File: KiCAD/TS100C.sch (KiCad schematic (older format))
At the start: 63 parts, among them J1 USB_C_Receptacle_USB2.0, J2 OLED_64x32, J3 A, J4 B, J5 DNP, P1 TC2030-CTX, Q1 SS8050, Q2 DMP3017SFG, SW1 key1, SW2 key2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

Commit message: fixed STM
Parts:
- U4: value STM32F072C8Ux -> STM32F072CBUx
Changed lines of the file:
@@
 EESchema Schematic File Version 4
 LIBS:TS100C-cache
-EELAYER 26 0
+EELAYER 30 0
 EELAYER END
 $Descr A3 16535 11693
@@
 P 7450 2700
 F 0 "U4" H 6900 4150 50  0000 C CNN
-F 1 "STM32F072C8Ux" H 8000 4150 50  0000 C CNN
+F 1 "STM32F072CBUx" H 8000 4150 50  0000 C CNN
 F 2 "Package_DFN_QFN:QFN-48-1EP_7x7mm_P0.5mm_EP5.6x5.6mm" H 6850 1300 50  0001 R CNN
 F 3 "http://www.st.com/st-web-ui/static/active/en/resource/technical/document/datasheet/DM00090510.pdf" H 7450 2700 50  0001 C CNN

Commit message: production files
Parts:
- U3: value STUSB4500 -> STUSB4500QTR
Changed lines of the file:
@@
 P 4300 7900
 F 0 "U3" H 4600 7150 50  0000 C CNN
-F 1 "STUSB4500" H 4600 7250 50  0000 C CNN
+F 1 "STUSB4500QTR" H 4600 7250 50  0000 C CNN
 F 2 "Package_DFN_QFN:QFN-24-1EP_4x4mm_P0.5mm_EP2.7x2.7mm" H 4300 7900 50  0001 C CNN
 F 3 "" H 4300 7900 50  0001 C CNN

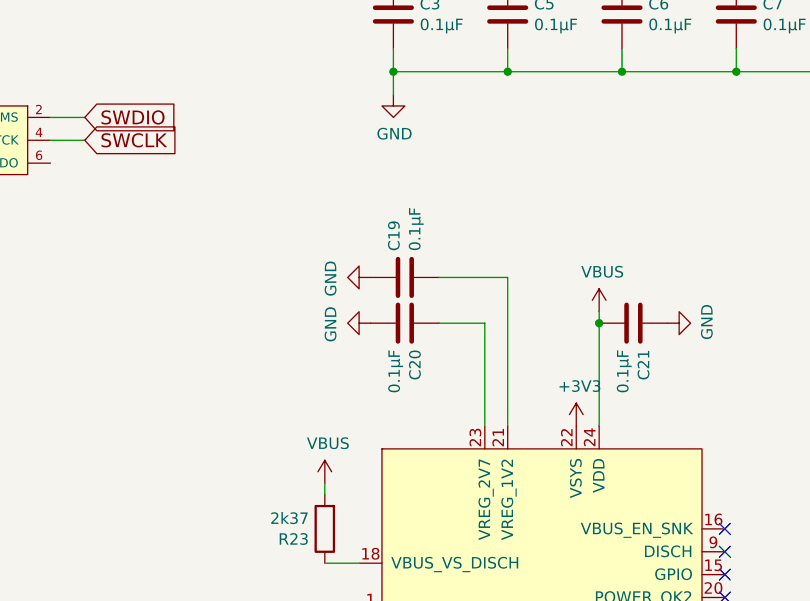
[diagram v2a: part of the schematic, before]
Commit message: updated cap values
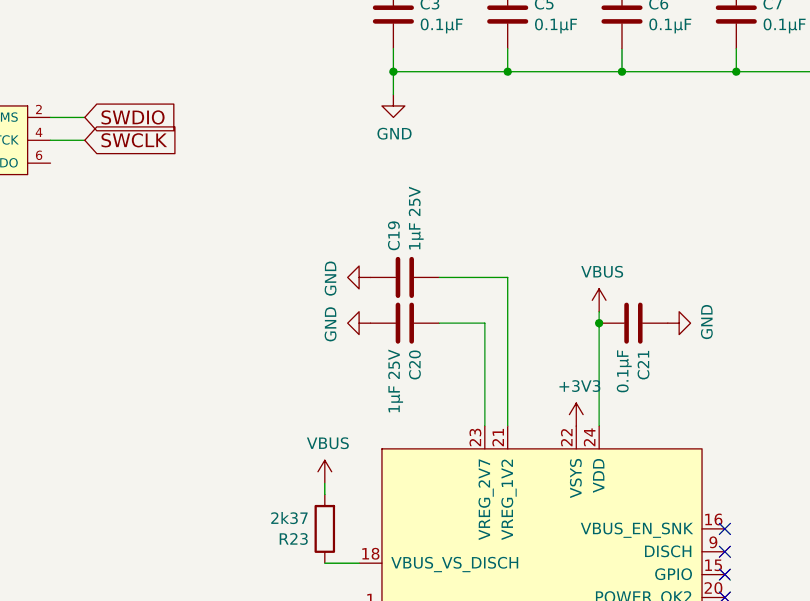
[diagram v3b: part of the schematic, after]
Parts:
- C19, C20: value 0.1μF -> 1μF 25V
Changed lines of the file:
@@
 P 3700 6500
 F 0 "C20" H 3815 6546 50  0000 L CNN
-F 1 "0.1μF" H 3815 6455 50  0000 L CNN
+F 1 "1μF 25V" H 3815 6455 50  0000 L CNN
 F 2 "Capacitor_SMD:C_0402_1005Metric" H 3738 6350 50  0001 C CNN
 F 3 "~" H 3700 6500 50  0001 C CNN
@@
 P 3700 6300
 F 0 "C19" H 3815 6346 50  0000 L CNN
-F 1 "0.1μF" H 3815 6255 50  0000 L CNN
+F 1 "1μF 25V" H 3815 6255 50  0000 L CNN
 F 2 "Capacitor_SMD:C_0402_1005Metric" H 3738 6150 50  0001 C CNN
 F 3 "~" H 3700 6300 50  0001 C CNN

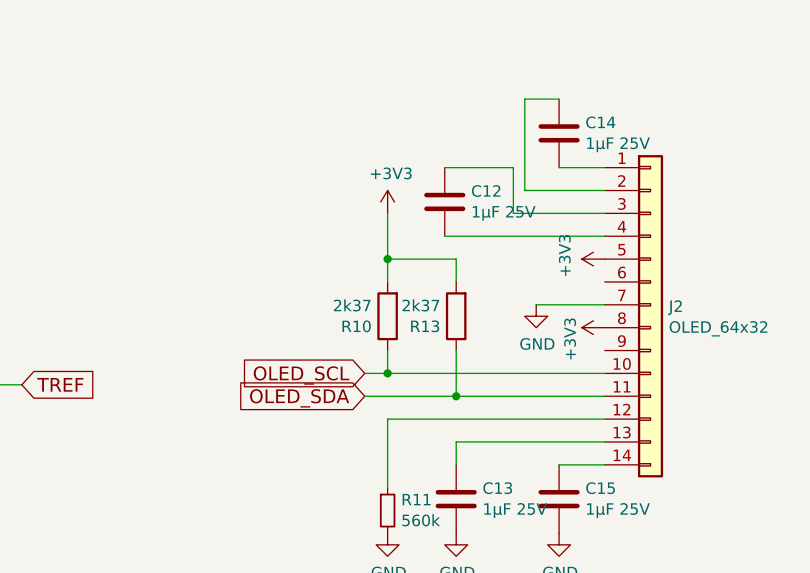
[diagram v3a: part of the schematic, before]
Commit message: optimized TC & Display connector, added pullup
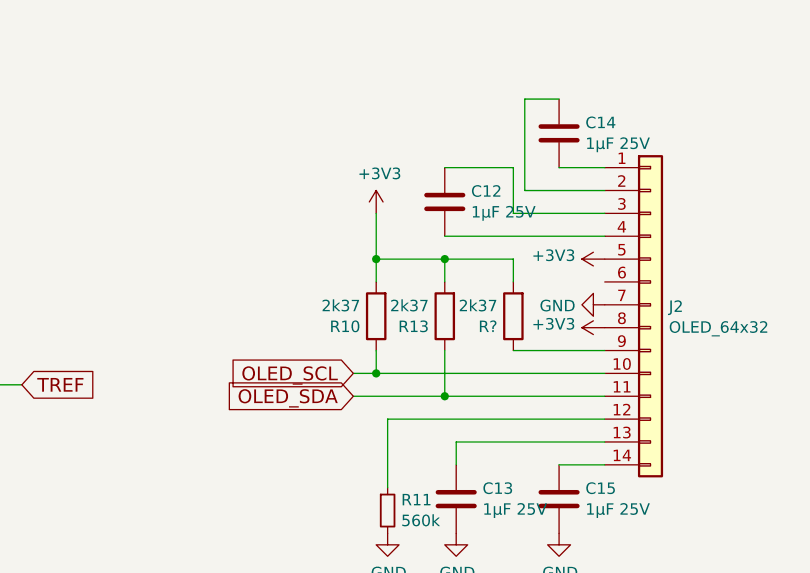
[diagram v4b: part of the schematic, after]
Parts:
- added R?: 2k37, Resistor_SMD:R_0402_1005Metric, symbol Device:R
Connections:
- net +3V3: now also R?.2
- net at J2.9 (Pin_9): now also R?.1
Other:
- moved on the sheet: R10, R13
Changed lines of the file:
@@
 EESchema Schematic File Version 4
-LIBS:TS100C-cache
 EELAYER 30 0
 EELAYER END
@@
 	13000 7600 13950 7600
 Wire Wire Line
-	12900 7500 13300 7500
-Wire Wire Line
-	12900 7400 13000 7400
-Wire Wire Line
-	13000 7400 13000 7300
-Wire Wire Line
-	13300 7500 13300 7300
-Wire Wire Line
-	13000 6900 13300 6900
-Wire Wire Line
-	13300 6900 13300 7000
-Connection ~ 13000 6900
-Wire Wire Line
-	13000 6900 13000 7000
+	12850 7500 13250 7500
+Wire Wire Line
+	12850 7400 12950 7400
+Wire Wire Line
+	12950 7400 12950 7300
+Wire Wire Line
+	13250 7500 13250 7300
+Wire Wire Line
+	12950 6900 13250 6900
+Wire Wire Line
+	13250 6900 13250 7000
+Connection ~ 12950 6900
+Wire Wire Line
+	12950 6900 12950 7000
 $Comp
 L Device:R R10
 U 1 1 5BF4CB02
-P 13000 7150
-F 0 "R10" H 13069 7196 50  0000 L CNN
-F 1 "2k37" H 13069 7105 50  0000 L CNN
-F 2 "Resistor_SMD:R_0402_1005Metric" V 12930 7150 50  0001 C CNN
-F 3 "~" H 13000 7150 50  0001 C CNN
-	1    13000 7150
+P 12950 7150
+F 0 "R10" H 13019 7196 50  0000 L CNN
+F 1 "2k37" H 13019 7105 50  0000 L CNN
+F 2 "Resistor_SMD:R_0402_1005Metric" V 12880 7150 50  0001 C CNN
+F 3 "~" H 12950 7150 50  0001 C CNN
+	1    12950 7150
 	-1   0    0    1
 $EndComp
@@
 L Device:R R13
 U 1 1 5BF4CB09
-P 13300 7150
-F 0 "R13" H 13369 7196 50  0000 L CNN
-F 1 "2k37" H 13369 7105 50  0000 L CNN
-F 2 "Resistor_SMD:R_0402_1005Metric" V 13230 7150 50  0001 C CNN
-F 3 "~" H 13300 7150 50  0001 C CNN
-	1    13300 7150
+P 13250 7150
+F 0 "R13" H 13319 7196 50  0000 L CNN
+F 1 "2k37" H 13319 7105 50  0000 L CNN
+F 2 "Resistor_SMD:R_0402_1005Metric" V 13180 7150 50  0001 C CNN
+F 3 "~" H 13250 7150 50  0001 C CNN
+	1    13250 7150
 	-1   0    0    1
 $EndComp
-Text GLabel 12900 7400 0    60   Input ~ 0
+Text GLabel 12850 7400 0    60   Input ~ 0
 OLED_SCL
-Text GLabel 12900 7500 0    60   Input ~ 0
+Text GLabel 12850 7500 0    60   Input ~ 0
 OLED_SDA
-Connection ~ 13000 7400
-Connection ~ 13300 7500
+Connection ~ 12950 7400
+Connection ~ 13250 7500
 $Comp
 L power:+3V3 #PWR0132
@@
 P 13950 7200
 F 0 "#PWR0132" H 13950 7050 50  0001 C CNN
-F 1 "+3V3" H 13900 7350 50  0000 C CNN
+F 1 "+3V3" V 13965 7328 50  0000 L CNN
 F 2 "" H 13950 7200 50  0001 C CNN
 F 3 "" H 13950 7200 50  0001 C CNN
@@
 P 13950 6900
 F 0 "#PWR0133" H 13950 6750 50  0001 C CNN
-F 1 "+3V3" H 13965 7073 50  0000 C CNN
+F 1 "+3V3" V 13965 7028 50  0000 L CNN
 F 2 "" H 13950 6900 50  0001 C CNN
 F 3 "" H 13950 6900 50  0001 C CNN
@@
 L power:GND #PWR?
 U 1 1 5BF71285
-P 13650 7100
+P 13950 7100
 AR Path="/588FB1D7/5BF71285" Ref="#PWR?"  Part="1"
 AR Path="/588FD270/5BF71285" Ref="#PWR?"  Part="1"
 AR Path="/5BF71285" Ref="#PWR0134"  Part="1"
-F 0 "#PWR0134" H 13650 6850 50  0001 C CNN
-F 1 "GND" H 13655 6927 50  0000 C CNN
-F 2 "" H 13650 7100 50  0001 C CNN
-F 3 "" H 13650 7100 50  0001 C CNN
-	1    13650 7100
-	1    0    0    -1
-$EndComp
-Wire Wire Line
-	13950 7100 13650 7100
+F 0 "#PWR0134" H 13950 6850 50  0001 C CNN
+F 1 "GND" V 13955 6972 50  0000 R CNN
+F 2 "" H 13950 7100 50  0001 C CNN
+F 3 "" H 13950 7100 50  0001 C CNN
+	1    13950 7100
+	0    1    1    0
+$EndComp
 $Comp
 L Device:C C?
@@
 Wire Wire Line
 	13600 6200 13750 6200
-Wire Wire Line
-	13000 7400 13950 7400
-Wire Wire Line
-	13300 7500 13950 7500
 Wire Wire Line
 	13950 6800 13250 6800
@@
 L power:+3V3 #PWR0148
 U 1 1 5D3A56D4
-P 13000 6700
-F 0 "#PWR0148" H 13000 6550 50  0001 C CNN
-F 1 "+3V3" H 13015 6873 50  0000 C CNN
-F 2 "" H 13000 6700 50  0001 C CNN
-F 3 "" H 13000 6700 50  0001 C CNN
-	1    13000 6700
-	1    0    0    -1
-$EndComp
-Wire Wire Line
-	13000 6700 13000 6900
+P 12950 6700
+F 0 "#PWR0148" H 12950 6550 50  0001 C CNN
+F 1 "+3V3" H 12965 6873 50  0000 C CNN
+F 2 "" H 12950 6700 50  0001 C CNN
+F 3 "" H 12950 6700 50  0001 C CNN
+	1    12950 6700
+	1    0    0    -1
+$EndComp
+Wire Wire Line
+	12950 6700 12950 6900
 Text GLabel 2150 2450 2    60   Input ~ 0
 CC1
 Text GLabel 2150 2550 2    60   Input ~ 0
 CC2
+$Comp
+L Device:R R?
+U 1 1 5E3425E7
+P 13550 7150
+F 0 "R?" H 13619 7196 50  0000 L CNN
+F 1 "2k37" H 13619 7105 50  0000 L CNN
+F 2 "Resistor_SMD:R_0402_1005Metric" V 13480 7150 50  0001 C CNN
+F 3 "~" H 13550 7150 50  0001 C CNN
+	1    13550 7150
+	-1   0    0    1
+$EndComp
+Wire Wire Line
+	13250 7500 13950 7500
+Wire Wire Line
+	12950 7400 13950 7400
+Wire Wire Line
+	13950 7300 13550 7300
+Wire Wire Line
+	13550 7000 13550 6900
+Wire Wire Line
+	13550 6900 13250 6900
+Connection ~ 13250 6900
 $EndSCHEMATC
